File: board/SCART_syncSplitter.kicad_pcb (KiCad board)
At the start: 2 copper layers, 76.1 x 58 mm, 34 parts, among them J1 SCART-F, J2 VGA Out, J3 POWER IN, J4 HSync Selector, J5 Audio Out, U1 LMH1981, U2 L7805

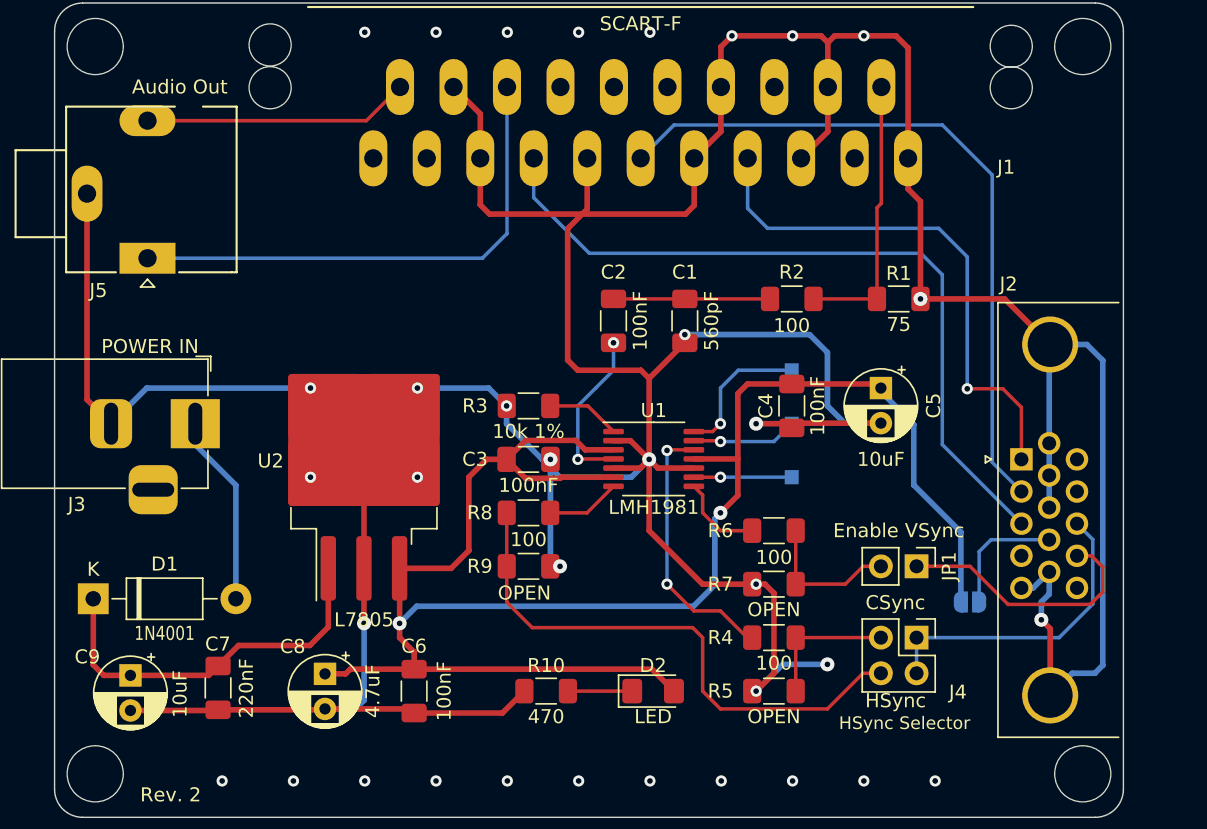
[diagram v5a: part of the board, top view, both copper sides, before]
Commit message: Add rev.2 board
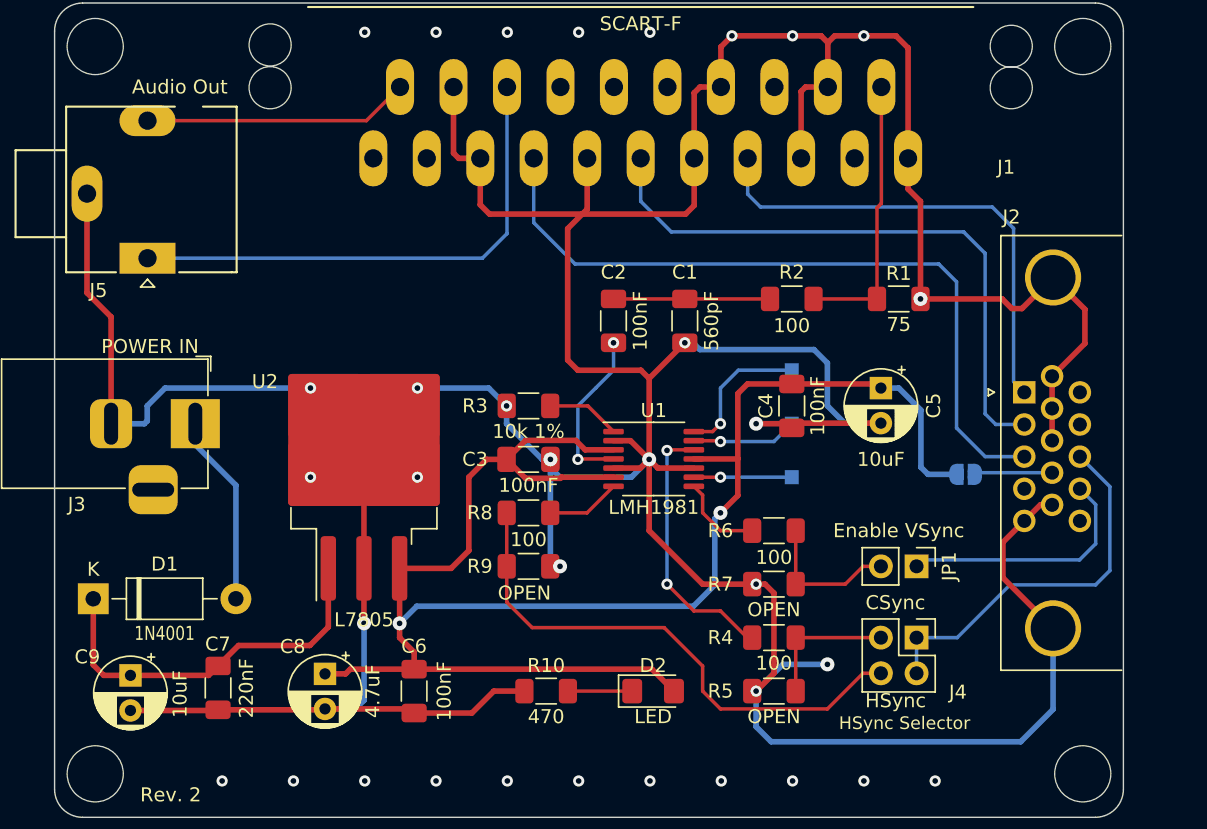
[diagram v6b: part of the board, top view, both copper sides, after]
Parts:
- moved JP2 9.10 mm to (167.3, 92.5)
- moved J2 4.78 mm to (171.4, 86.6)
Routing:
- net /S_GREEN: track 50.9 -> 43.7 mm
- net VCC: track 133.1 -> 126.0 mm
- net GND: track 360.0 -> 365.3 mm, vias 35 -> 34
- net Net-(J4-Pin_1): track 22.3 -> 27.3 mm
- net /S_RED: track 38.2 -> 34.5 mm, vias 1 -> 0
- net Net-(JP2-B): track 8.93 -> 5.55 mm
- net /S_BLUE: track 54.3 -> 52.5 mm
- net /HSync_OUT: track 39.5 -> 38.3 mm
- net Net-(JP1-A): track 18.7 -> 17.8 mm
